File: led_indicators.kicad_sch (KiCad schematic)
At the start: 15 parts

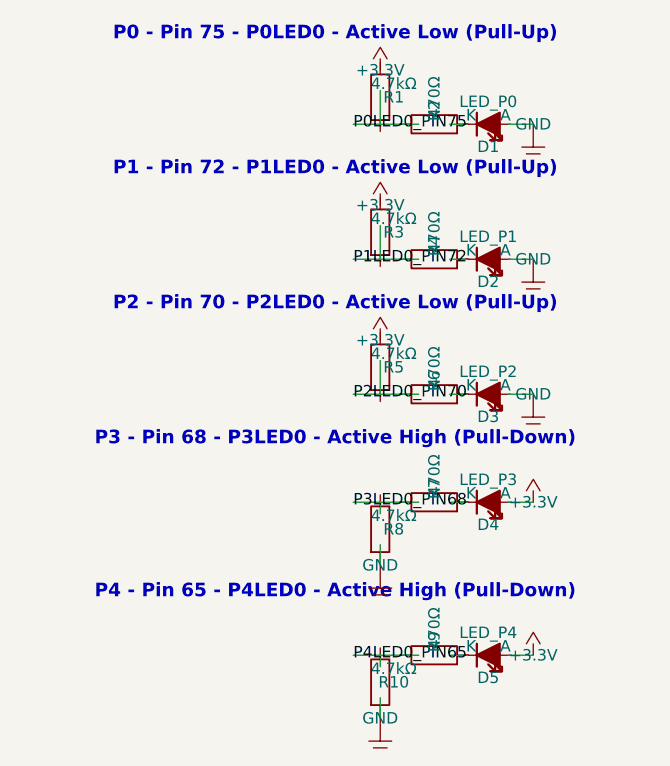
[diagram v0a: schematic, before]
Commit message: Fix kicad_sch: remove invalid comments, fix syntax errors
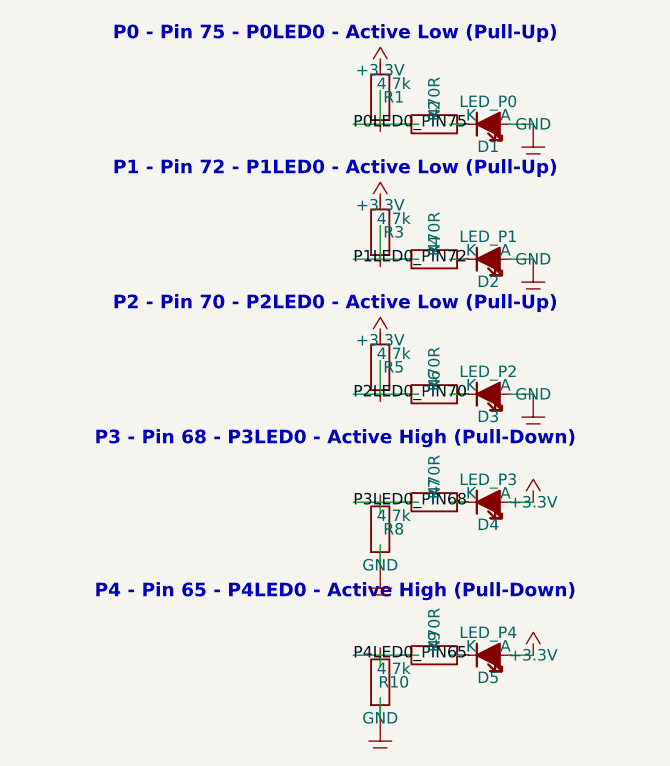
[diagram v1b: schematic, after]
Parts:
- R1, R10, R3, R5, R8: value 4.7kΩ -> 4.7k
- R2, R4, R6, R7, R9: value 470Ω -> 470R
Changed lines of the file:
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@@
     (rev "1.0")
     (comment 1 "Link/Act LEDs para los 5 puertos")
-    (comment 2 "Puertos 0,1,2: Active Low (Pull-Up 4.7k) | Puertos 3,4: Active High (Pull-Down 4.7k)")
-    (comment 3 "Resistencia serie: 470 ohm | Sin Gigabit, solo Link/Act")
+    (comment 2 "Puertos 0,1,2: Active Low | Puertos 3,4: Active High")
+    (comment 3 "Resistencia serie: 470R | Pull: 4.7k | Sin Gigabit")
   )
-  ;; =========================================
-  ;; PUERTO 0 - Pin 75 - P0LED0 - Active Low
-  ;; =========================================
   (text "P0 - Pin 75 - P0LED0 - Active Low (Pull-Up)" (at 3 3 0)
     (effects (font (size 1.5 1.5) bold)))
@@
   (symbol (lib_id "Device:R") (at 8 10 0) (unit 1)
     (property "Reference" "R1" (at 9.5 10 0) (effects (font (size 1.27 1.27))))
-    (property "Value" "4.7kΩ" (at 9.5 8.5 0) (effects (font (size 1.27 1.27)))))
+    (property "Value" "4.7k" (at 9.5 8.5 0) (effects (font (size 1.27 1.27)))))
   (symbol (lib_id "Device:R") (at 14 13 90) (unit 1)
     (property "Reference" "R2" (at 14 11.5 0) (effects (font (size 1.27 1.27))))
-    (property "Value" "470Ω" (at 14 10 0) (effects (font (size 1.27 1.27)))))
+    (property "Value" "470R" (at 14 10 0) (effects (font (size 1.27 1.27)))))
   (symbol (lib_id "Device:LED") (at 20 13 0) (unit 1)
     (property "Reference" "D1" (at 20 15.5 0) (effects (font (size 1.27 1.27))))
@@
   (wire (pts (xy 15.73 13) (xy 17.73 13)))
   (wire (pts (xy 22.27 13) (xy 25 13)))
-  (label "P0LED0_PIN75" (at 5 13 0)
-    (effects (font (size 1.27 1.27))))
+  (label "P0LED0_PIN75" (at 5 13 0) (effects (font (size 1.27 1.27))))
   (wire (pts (xy 5 13) (xy 8 13)))
-  ;; =========================================
-  ;; PUERTO 1 - Pin 72 - P1LED0 - Active Low
-  ;; =========================================
   (text "P1 - Pin 72 - P1LED0 - Active Low (Pull-Up)" (at 3 18 0)
     (effects (font (size 1.5 1.5) bold)))
@@
   (symbol (lib_id "Device:R") (at 8 25 0) (unit 1)
     (property "Reference" "R3" (at 9.5 25 0) (effects (font (size 1.27 1.27))))
-    (property "Value" "4.7kΩ" (at 9.5 23.5 0) (effects (font (size 1.27 1.27)))))
+    (property "Value" "4.7k" (at 9.5 23.5 0) (effects (font (size 1.27 1.27)))))
   (symbol (lib_id "Device:R") (at 14 28 90) (unit 1)
     (property "Reference" "R4" (at 14 26.5 0) (effects (font (size 1.27 1.27))))
-    (property "Value" "470Ω" (at 14 25 0) (effects (font (size 1.27 1.27)))))
+    (property "Value" "470R" (at 14 25 0) (effects (font (size 1.27 1.27)))))
   (symbol (lib_id "Device:LED") (at 20 28 0) (unit 1)
     (property "Reference" "D2" (at 20 30.5 0) (effects (font (size 1.27 1.27))))
@@
   (wire (pts (xy 15.73 28) (xy 17.73 28)))
   (wire (pts (xy 22.27 28) (xy 25 28)))
-  (label "P1LED0_PIN72" (at 5 28 0)
-    (effects (font (size 1.27 1.27))))
+  (label "P1LED0_PIN72" (at 5 28 0) (effects (font (size 1.27 1.27))))
   (wire (pts (xy 5 28) (xy 8 28)))
-  ;; =========================================
-  ;; PUERTO 2 - Pin 70 - P2LED0 - Active Low
-  ;; =========================================
   (text "P2 - Pin 70 - P2LED0 - Active Low (Pull-Up)" (at 3 33 0)
     (effects (font (size 1.5 1.5) bold)))
@@
   (symbol (lib_id "Device:R") (at 8 40 0) (unit 1)
     (property "Reference" "R5" (at 9.5 40 0) (effects (font (size 1.27 1.27))))
-    (property "Value" "4.7kΩ" (at 9.5 38.5 0) (effects (font (size 1.27 1.27)))))
+    (property "Value" "4.7k" (at 9.5 38.5 0) (effects (font (size 1.27 1.27)))))
   (symbol (lib_id "Device:R") (at 14 43 90) (unit 1)
     (property "Reference" "R6" (at 14 41.5 0) (effects (font (size 1.27 1.27))))
-    (property "Value" "470Ω" (at 14 40 0) (effects (font (size 1.27 1.27)))))
+    (property "Value" "470R" (at 14 40 0) (effects (font (size 1.27 1.27)))))
   (symbol (lib_id "Device:LED") (at 20 43 0) (unit 1)
     (property "Reference" "D3" (at 20 45.5 0) (effects (font (size 1.27 1.27))))
@@
   (wire (pts (xy 15.73 43) (xy 17.73 43)))
   (wire (pts (xy 22.27 43) (xy 25 43)))
-  (label "P2LED0_PIN70" (at 5 43 0)
-    (effects (font (size 1.27 1.27))))
+  (label "P2LED0_PIN70" (at 5 43 0) (effects (font (size 1.27 1.27))))
   (wire (pts (xy 5 43) (xy 8 43)))
-  ;; ============================================
-  ;; PUERTO 3 - Pin 68 - P3LED0 - Active High
-  ;; ============================================
   (text "P3 - Pin 68 - P3LED0 - Active High (Pull-Down)" (at 3 48 0)
     (effects (font (size 1.5 1.5) bold)))
@@
   (symbol (lib_id "Device:R") (at 14 55 90) (unit 1)
     (property "Reference" "R7" (at 14 53.5 0) (effects (font (size 1.27 1.27))))
-    (property "Value" "470Ω" (at 14 52 0) (effects (font (size 1.27 1.27)))))
+    (property "Value" "470R" (at 14 52 0) (effects (font (size 1.27 1.27)))))
   (symbol (lib_id "Device:R") (at 8 58 0) (unit 1)
     (property "Reference" "R8" (at 9.5 58 0) (effects (font (size 1.27 1.27))))
-    (property "Value" "4.7kΩ" (at 9.5 56.5 0) (effects (font (size 1.27 1.27)))))
+    (property "Value" "4.7k" (at 9.5 56.5 0) (effects (font (size 1.27 1.27)))))
   (symbol (lib_id "power:GND") (at 8 62 0) (unit 1)
     (property "Reference" "#PWR08" (at 8 62 0) (effects (font (size 1.27 1.27)) hide))
@@
   (wire (pts (xy 15.73 55) (xy 17.73 55)))
   (wire (pts (xy 22.27 55) (xy 25 55)))
-  (label "P3LED0_PIN68" (at 5 55 0)
-    (effects (font (size 1.27 1.27))))
+  (label "P3LED0_PIN68" (at 5 55 0) (effects (font (size 1.27 1.27))))
   (wire (pts (xy 5 55) (xy 8 55)))
-  ;; ============================================
-  ;; PUERTO 4 - Pin 65 - P4LED0 - Active High
-  ;; ============================================
   (text "P4 - Pin 65 - P4LED0 - Active High (Pull-Down)" (at 3 65 0)
     (effects (font (size 1.5 1.5) bold)))
@@
   (symbol (lib_id "Device:R") (at 14 72 90) (unit 1)
     (property "Reference" "R9" (at 14 70.5 0) (effects (font (size 1.27 1.27))))
-    (property "Value" "470Ω" (at 14 69 0) (effects (font (size 1.27 1.27)))))
+    (property "Value" "470R" (at 14 69 0) (effects (font (size 1.27 1.27)))))
   (symbol (lib_id "Device:R") (at 8 75 0) (unit 1)
     (property "Reference" "R10" (at 9.5 75 0) (effects (font (size 1.27 1.27))))
-    (property "Value" "4.7kΩ" (at 9.5 73.5 0) (effects (font (size 1.27 1.27)))))
+    (property "Value" "4.7k" (at 9.5 73.5 0) (effects (font (size 1.27 1.27)))))
   (symbol (lib_id "power:GND") (at 8 79 0) (unit 1)
     (property "Reference" "#PWR10" (at 8 79 0) (effects (font (size 1.27 1.27)) hide))
@@
   (wire (pts (xy 15.73 72) (xy 17.73 72)))
   (wire (pts (xy 22.27 72) (xy 25 72)))
-  (label "P4LED0_PIN65" (at 5 72 0)
-    (effects (font (size 1.27 1.27))))
+  (label "P4LED0_PIN65" (at 5 72 0) (effects (font (size 1.27 1.27))))
   (wire (pts (xy 5 72) (xy 8 72)))
 )
